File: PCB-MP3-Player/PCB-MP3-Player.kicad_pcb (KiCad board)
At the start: 2 copper layers, 72.6 x 80.8 mm, 26 parts, among them J1 Conn_01x02_Pin, J2 PCM5102A, J3 Oled, J4 Conn_01x06_Pin, J5 Conn_01x02_Pin, J6 Conn_01x03_Pin, J7 Conn_01x03_Pin, SW1 SW_Push, SW2 SW_Push, SW3 SW_Push, SW4 SW_Push, SW5 SW_Push

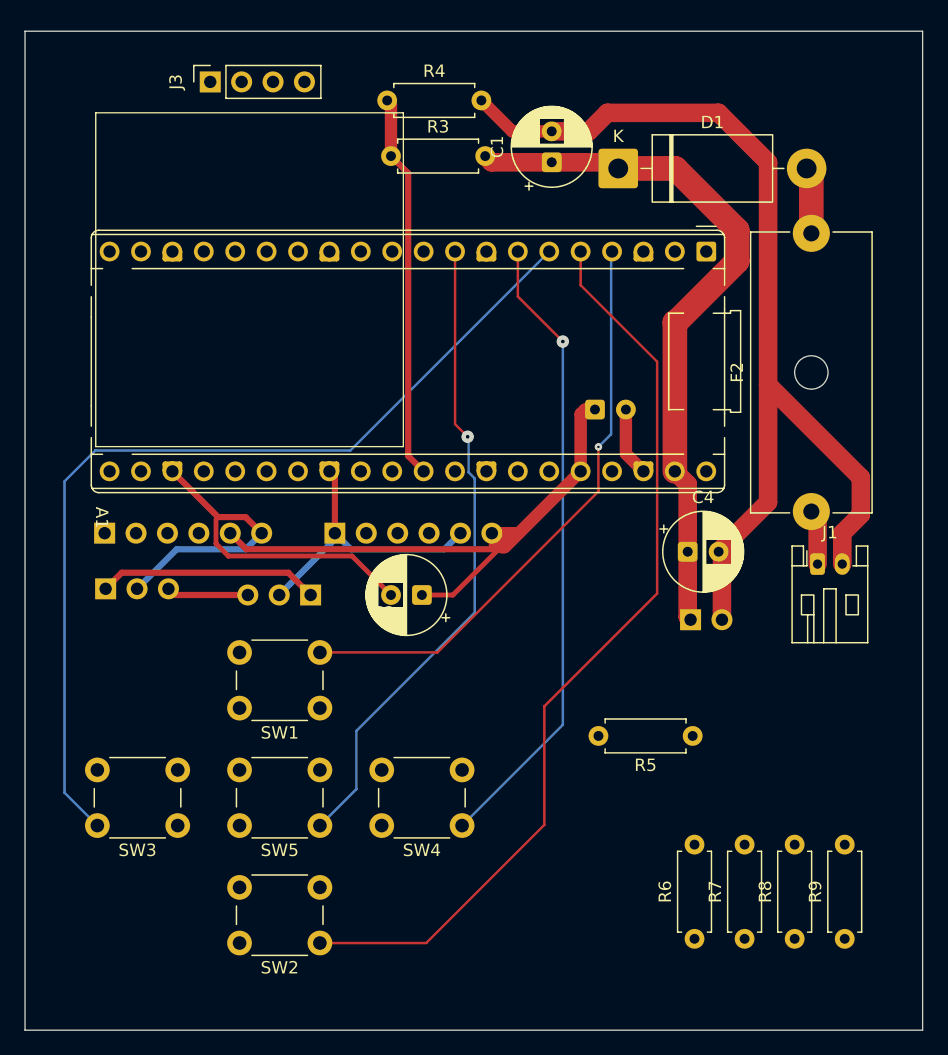
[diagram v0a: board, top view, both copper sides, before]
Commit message: connected oled
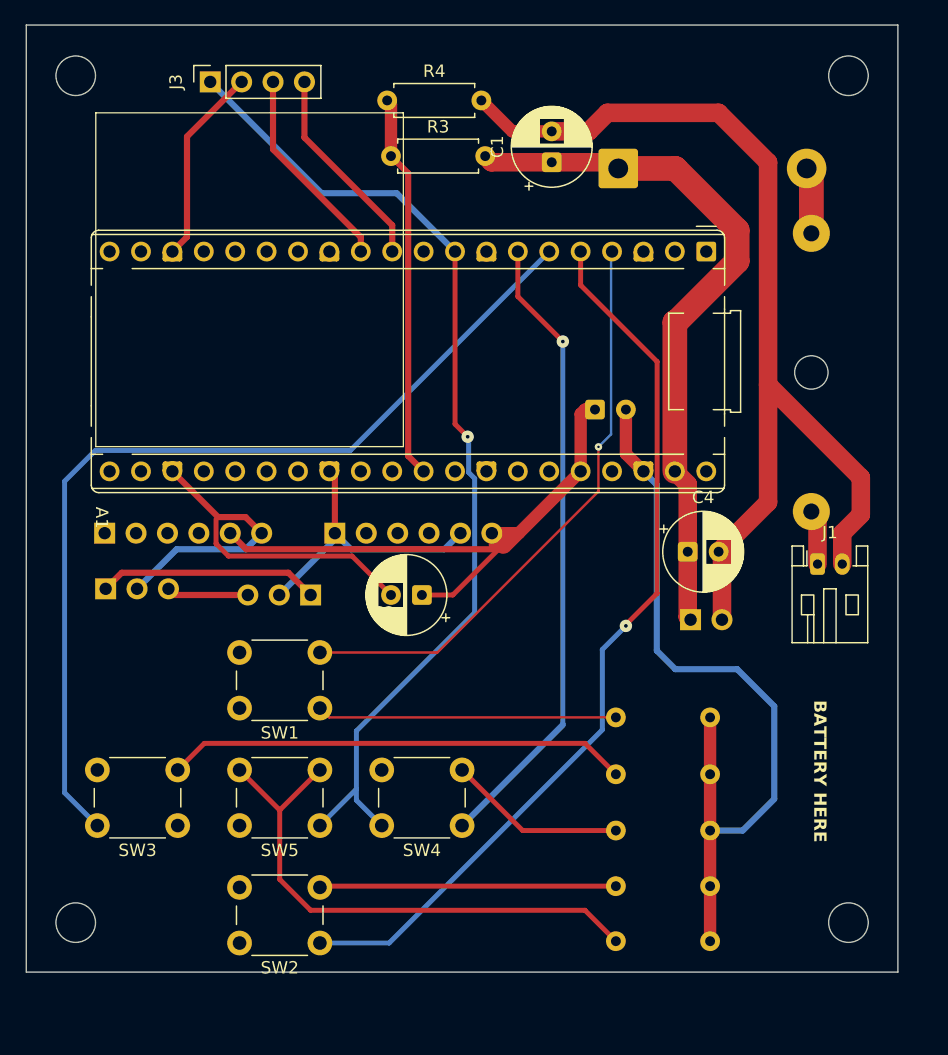
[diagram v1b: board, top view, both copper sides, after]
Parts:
- added REF**: MountingHole_3.2mm_M3_DIN965, MountingHole:MountingHole_3.2mm_M3_DIN965, F.Cu at (132.5, 157.5)
- added REF**: MountingHole_3.2mm_M3_DIN965, MountingHole:MountingHole_3.2mm_M3_DIN965, F.Cu at (195.0, 89.0)
- added REF**: MountingHole_3.2mm_M3_DIN965, MountingHole:MountingHole_3.2mm_M3_DIN965, F.Cu at (195.0, 157.5)
- added REF**: MountingHole_3.2mm_M3_DIN965, MountingHole:MountingHole_3.2mm_M3_DIN965, F.Cu at (132.5, 89.0)
- D1, F2, R5, R6, R7, R8, R9: moved to B.Cu
- moved R9 21.0 mm to (183.8, 140.9), turned to 180 degrees
- moved R5 16.7 mm to (183.8, 159.0)
- moved R8 15.0 mm to (183.8, 145.5), turned to 180 degrees
- moved R7 9.19 mm to (183.8, 150.1), turned to 180 degrees
- moved R6 4.44 mm to (183.8, 154.6), turned to 180 degrees
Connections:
- SW1 pad 1: Net-(R5-Pad2) -> Net-(R9-Pad2)
- SW3 pad 2: Net-(R7-Pad2) -> Net-(R8-Pad2)
- SW4 pad 2: Net-(R8-Pad2) -> Net-(R7-Pad2)
- SW5 pad 2: Net-(R9-Pad2) -> Net-(R5-Pad2)
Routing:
- net GND: track 68.2 -> 142.4 mm
- net Net-(R5-Pad2): track 0.00 -> 44.1 mm
- net Net-(R8-Pad2): track 0.00 -> 37.4 mm
- net +3.3V: track 360.2 -> 387.7 mm, vias 3 -> 4
- net Net-(R9-Pad2): track 0.00 -> 24.3 mm
- net Net-(R6-Pad2): track 0.00 -> 24.0 mm
- net /SDA: track 0.00 -> 16.7 mm
- net /SCL: track 0.00 -> 16.7 mm
- net Net-(R7-Pad2): track 0.00 -> 14.5 mm
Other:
- board size 72.6 x 80.8 mm -> 70.5 x 76.6 mm
- board text added: "BATTERY HERE"

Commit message: pcb changes
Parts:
- removed C4: 100microFarad, Capacitor_THT:CP_Radial_D6.3mm_P2.50mm
- removed J5: Conn_01x02_Pin, Connector_PinSocket_2.54mm:PinSocket_1x02_P2.54mm_Vertical
- removed J6, J7: Conn_01x03_Pin, Connector_PinSocket_2.54mm:PinSocket_1x03_P2.54mm_Vertical
- C1, C2, J1, R3, R4: moved to B.Cu
- C3: moved to F.Cu
- moved R4 7.62 mm to (165.3, 91.0), turned to 180 degrees
- moved C2 2.68 mm to (157.8, 131.0), turned to 0 degrees
- moved J1 2.06 mm to (194.5, 128.0), turned to 180 degrees
- moved R3 0.59 mm to (157.7, 95.0)
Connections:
- C1 pad 2: -BATT -> GND
- C2 pad 1: +3.3V -> GND
- C2 pad 2: GND -> +3.3V
- J1 pad 2: -BATT -> GND
- R4 pad 1: /ADC_BAT -> GND
- R4 pad 2: -BATT -> /ADC_BAT
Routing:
- net -BATT: track 83.5 -> 0.00 mm
- net GND: track 142.4 -> 218.1 mm
- net /L_AUDIO: track 17.9 -> 0.00 mm
- net /LRCK: track 0.00 -> 12.7 mm
- net +BATT: track 57.0 -> 45.0 mm
- net /BCK: track 0.00 -> 10.1 mm
- net /MISO: track 0.00 -> 9.29 mm
- net /SCK: track 0.00 -> 7.55 mm
- net /MOSI: track 0.00 -> 7.55 mm
- net /R_AUDIO: track 6.63 -> 0.00 mm
- net /DIN1: track 0.00 -> 6.23 mm
- net /CS: track 0.00 -> 6.22 mm

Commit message: Devlog #6
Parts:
- A1: moved to B.Cu
- moved A1 50.5 mm to (133.0, 104.0)
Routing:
- net /CS: track 6.22 -> 59.6 mm
- net /SCK: track 7.55 -> 54.6 mm
- net /MISO: track 9.29 -> 46.8 mm
- net /MOSI: track 7.55 -> 38.2 mm
- net +3.3V: track 387.7 -> 415.3 mm, vias 4 -> 5
- net GND: track 218.1 -> 191.2 mm
- net +BATT: track 45.0 -> 63.9 mm
- net /BCK: track 10.1 -> 18.3 mm
- net Net-(R9-Pad2): track 24.3 -> 30.8 mm
- net Net-(R8-Pad2): track 37.4 -> 43.9 mm
- net Net-(R7-Pad2): track 14.5 -> 21.0 mm
- net Net-(R6-Pad2): track 24.0 -> 30.5 mm
- net /LRCK: track 12.7 -> 6.71 mm
- net /SCL: track 16.7 -> 19.7 mm
- net /ADC_BAT: track 31.7 -> 33.7 mm
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
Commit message: Devlog 7
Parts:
- C2: moved to F.Cu
- J4: footprint Connector_PinSocket_2.54mm:PinSocket_1x06_P2.54mm_Vertical -> Connector_JST:JST_SHL_SM06B-SHLS-TF_1x06-1MP_P1.00mm_Horizontal
- moved C2 15.3 mm to (172.0, 125.3), turned to -90 degrees
- moved J4 3.62 mm to (135.6, 129.6)
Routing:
- net +3.3V: track 415.3 -> 441.2 mm
- net GND: track 191.2 -> 211.1 mm
- net /MISO: track 46.8 -> 56.7 mm, vias 0 -> 1
- net /MOSI: track 38.2 -> 45.8 mm, vias 0 -> 1
- net /SCK: track 54.6 -> 57.2 mm, vias 0 -> 1
- net /CS: track 59.6 -> 61.0 mm, vias 0 -> 1

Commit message: Adding renders, readme, etc.
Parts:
- F2: value Littelfuse 02301002H -> 520.620
- J4: footprint Connector_JST:JST_SHL_SM06B-SHLS-TF_1x06-1MP_P1.00mm_Horizontal -> Connector_JST:JST_SH_SM06B-SRSS-TB_1x06-1MP_P1.00mm_Horizontal
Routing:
- net +3.3V: track 441.2 -> 442.1 mm
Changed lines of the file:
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@@
 		)
 	)
-	(footprint "Connector_JST:JST_SHL_SM06B-SHLS-TF_1x06-1MP_P1.00mm_Horizontal"
+	(footprint "Connector_JST:JST_SH_SM06B-SRSS-TB_1x06-1MP_P1.00mm_Horizontal"
 		(layer "B.Cu")
 		(at 135.55 129.55 -90)
-		(descr "JST SHL series connector, SM06B-SHLS-TF (http://www.jst-mfg.com/product/pdf/eng/eSHL.pdf)")
-		(tags "connector JST SHL horizontal")
+		(descr "JST SH series connector, SM06B-SRSS-TB (http://www.jst-mfg.com/product/pdf/eng/eSH.pdf)")
+		(tags "connector JST SH horizontal")
 		(property "Reference" "J4"
-			(at 0 3.5 90)
+			(at 0 3.98 90)
 			(layer "B.SilkS")
 			(effects
@@
 		)
 		(property "Value" "Conn_01x06_Pin"
-			(at 0 -4.2 90)
+			(at 0 -3.98 90)
 			(layer "B.Fab")
 			(effects
@@
 		(duplicate_pad_numbers_are_jumpers no)
 		(fp_line
-			(start -4.51 1.41)
-			(end -3.06 1.41)
+			(start -4.11 1.785)
+			(end -3.06 1.785)
 			(stroke
 				(width 0.12)
@@
 		)
 		(fp_line
-			(start -3.06 1.41)
-			(end -3.06 2.3)
+			(start -3.06 1.785)
+			(end -3.06 2.775)
 			(stroke
 				(width 0.12)
@@
 		)
 		(fp_line
-			(start 4.51 1.41)
-			(end 3.06 1.41)
+			(start 4.11 1.785)
+			(end 3.06 1.785)
 			(stroke
 				(width 0.12)
@@
 		)
 		(fp_line
-			(start -4.51 -0.34)
-			(end -4.51 1.41)
+			(start -4.11 -0.715)
+			(end -4.11 1.785)
 			(stroke
 				(width 0.12)
@@
 		)
 		(fp_line
-			(start 4.51 -0.34)
-			(end 4.51 1.41)
+			(start 4.11 -0.715)
+			(end 4.11 1.785)
 			(stroke
 				(width 0.12)
@@
 		)
 		(fp_line
-			(start -4.51 -2.56)
-			(end -4.51 -3.11)
+			(start -2.94 -2.685)
+			(end 2.94 -2.685)
 			(stroke
 				(width 0.12)
@@
 		)
 		(fp_line
-			(start -4.51 -3.11)
-			(end 4.51 -3.11)
+			(start -3.3 3.28)
+			(end 3.3 3.28)
 			(stroke
-				(width 0.12)
+				(width 0.05)
 				(type solid)
 			)
-			(layer "B.SilkS")
+			(layer "B.CrtYd")
 		)
 		(fp_line
-			(start 4.51 -3.11)
-			(end 4.51 -2.56)
+			(start 3.3 3.28)
+			(end 3.3 2.18)
 			(stroke
-				(width 0.12)
+				(width 0.05)
 				(type solid)
 			)
-			(layer "B.SilkS")
+			(layer "B.CrtYd")
+		)
+		(fp_line
+			(start -4.5 2.18)
+			(end -3.3 2.18)
+			(stroke
+				(width 0.05)
+				(type solid)
+			)
+			(layer "B.CrtYd")
+		)
+		(fp_line
+			(start -3.3 2.18)
+			(end -3.3 3.28)
+			(stroke
+				(width 0.05)
+				(type solid)
+			)
+			(layer "B.CrtYd")
+		)
+		(fp_line
+			(start 3.3 2.18)
+			(end 4.5 2.18)
+			(stroke
+				(width 0.05)
+				(type solid)
+			)
+			(layer "B.CrtYd")
+		)
+		(fp_line
+			(start 4.5 2.18)
+			(end 4.5 -0.47)
+			(stroke
+				(width 0.05)
+				(type solid)
+			)
+			(layer "B.CrtYd")
+		)
+		(fp_line
+			(start -4.9 -0.47)
+			(end -4.5 -0.47)
+			(stroke
+				(width 0.05)
+				(type solid)
+			)
+			(layer "B.CrtYd")
 		)
 		(fp_line
-			(start -3.3 2.8)
-			(end 3.3 2.8)
+			(start -4.5 -0.47)
+			(end -4.5 2.18)
 			(stroke
 				(width 0.05)
@@
 		)
 		(fp_line
-			(start 3.3 2.8)
-			(end 3.3 1.8)
+			(start 4.5 -0.47)
+			(end 4.9 -0.47)
 			(stroke
 				(width 0.05)
@@
 		)
 		(fp_line
-			(start -4.9 1.8)
-			(end -3.3 1.8)
+			(start 4.9 -0.47)
+			(end 4.9 -3.28)
 			(stroke
 				(width 0.05)
@@
 		)
 		(fp_line
-			(start -3.3 1.8)
-			(end -3.3 2.8)
+			(start -2.69 -3.08)
+			(end -2.69 -3.28)
 			(stroke
 				(width 0.05)
@@
 		)
 		(fp_line
-			(start 3.3 1.8)
-			(end 4.9 1.8)
+			(start 2.69 -3.08)
+			(end -2.69 -3.08)
 			(stroke
 				(width 0.05)
@@
 		)
 		(fp_line
-			(start 4.9 1.8)
-			(end 4.9 -3.5)
+			(start -4.9 -3.28)
+			(end -4.9 -0.47)
 			(stroke
 				(width 0.05)
@@
 		)
 		(fp_line
-			(start -4.9 -3.5)
-			(end -4.9 1.8)
+			(start -2.69 -3.28)
+			(end -4.9 -3.28)
 			(stroke
 				(width 0.05)
@@
 		)
 		(fp_line
-			(start 4.9 -3.5)
-			(end -4.9 -3.5)
+			(start 2.69 -3.28)
+			(end 2.69 -3.08)
 			(stroke
 				(width 0.05)
@@
 		)
 		(fp_line
-			(start -4.4 1.3)
-			(end 4.4 1.3)
+			(start 4.9 -3.28)
+			(end 2.69 -3.28)
+			(stroke
+				(width 0.05)
+				(type solid)
+			)
+			(layer "B.CrtYd")
+		)
+		(fp_line
+			(start -4 1.675)
+			(end 4 1.675)
 			(stroke
 				(width 0.1)
@@
 		)
 		(fp_line
-			(start -4.4 1.3)
-			(end -4.4 -3)
+			(start -4 1.675)
+			(end -4 -2.575)
 			(stroke
 				(width 0.1)
@@
 		)
 		(fp_line
-			(start -3 1.3)
-			(end -2.5 0.592893)
+			(start -3 1.675)
+			(end -2.5 0.967893)
 			(stroke
 				(width 0.1)
@@
 		)
 		(fp_line
-			(start 4.4 1.3)
-			(end 4.4 -3)
+			(start 4 1.675)
+			(end 4 -2.575)
 			(stroke
 				(width 0.1)
@@
 		)
 		(fp_line
-			(start -2.5 0.592893)
-			(end -2 1.3)
+			(start -2.5 0.967893)
+			(end -2 1.675)
 			(stroke
 				(width 0.1)
@@
 		)
 		(fp_line
-			(start -4.4 -3)
-			(end 4.4 -3)
+			(start -4 -2.575)
+			(end 4 -2.575)
 			(stroke
 				(width 0.1)
@@
 		)
 		(fp_text user "${REFERENCE}"
-			(at 0 -0.5 90)
+			(at 0 0 90)
 			(layer "B.Fab")
 			(effects
@@
 		)
 		(pad "1" smd roundrect
-			(at -2.5 1.675 270)
-			(size 0.6 1.25)
+			(at -2.5 2 270)
+			(size 0.6 1.55)
 			(layers "B.Cu" "B.Mask" "B.Paste")
 			(roundrect_rratio 0.25)
@@
 		)
 		(pad "2" smd roundrect
-			(at -1.5 1.675 270)
-			(size 0.6 1.25)
+			(at -1.5 2 270)
+			(size 0.6 1.55)
 			(layers "B.Cu" "B.Mask" "B.Paste")
 			(roundrect_rratio 0.25)
@@
 		)
 		(pad "3" smd roundrect
-			(at -0.5 1.675 270)
-			(size 0.6 1.25)
+			(at -0.5 2 270)
+			(size 0.6 1.55)
 			(layers "B.Cu" "B.Mask" "B.Paste")
 			(roundrect_rratio 0.25)
@@
 		)
 		(pad "4" smd roundrect
-			(at 0.5 1.675 270)
-			(size 0.6 1.25)
+			(at 0.5 2 270)
+			(size 0.6 1.55)
 			(layers "B.Cu" "B.Mask" "B.Paste")
 			(roundrect_rratio 0.25)
@@
 		)
 		(pad "5" smd roundrect
-			(at 1.5 1.675 270)
-			(size 0.6 1.25)
+			(at 1.5 2 270)
+			(size 0.6 1.55)
 			(layers "B.Cu" "B.Mask" "B.Paste")
 			(roundrect_rratio 0.25)
@@
 		)
 		(pad "6" smd roundrect
-			(at 2.5 1.675 270)
-			(size 0.6 1.25)
+			(at 2.5 2 270)
+			(size 0.6 1.55)
 			(layers "B.Cu" "B.Mask" "B.Paste")
 			(roundrect_rratio 0.25)
@@
 		)
 		(pad "MP" smd roundrect
-			(at -3.95 -1.45 270)
-			(size 0.9 1.7)
+			(at -3.8 -1.875 270)
+			(size 1.2 1.8)
 			(layers "B.Cu" "B.Mask" "B.Paste")
-			(roundrect_rratio 0.25)
+			(roundrect_rratio 0.208333)
 		)
 		(pad "MP" smd roundrect
-			(at 3.95 -1.45 270)
-			(size 0.9 1.7)
+			(at 3.8 -1.875 270)
+			(size 1.2 1.8)
 			(layers "B.Cu" "B.Mask" "B.Paste")
-			(roundrect_rratio 0.25)
+			(roundrect_rratio 0.208333)
 		)
 		(embedded_fonts no)
-		(model "${KICAD10_3DMODEL_DIR}/Connector_JST.3dshapes/JST_SHL_SM06B-SHLS-TF_1x06-1MP_P1.00mm_Horizontal.step"
+		(model "${KICAD10_3DMODEL_DIR}/Connector_JST.3dshapes/JST_SH_SM06B-SRSS-TB_1x06-1MP_P1.00mm_Horizontal.step"
 			(offset
 				(xyz 0 0 0)
@@
 			)
 		)
-		(property "Value" "Littelfuse 02301002H"
+		(property "Value" "520.620"
 			(at 11.25 -6 90)
 			(layer "B.Fab")
@@
 	)
 	(segment
-		(start 132.5 130.299999)
-		(end 132.5 126.5)
-		(width 0.5)
-		(layer "B.Cu")
-		(net "+3.3V")
-	)
-	(segment
 		(start 155 134.5)
 		(end 155 135.5)
@@
 	)
 	(segment
+		(start 132.7 131.05)
+		(end 133.55 131.05)
+		(width 0.4)
+		(layer "B.Cu")
+		(net "+3.3V")
+	)
+	(segment
 		(start 132.5 126.5)
 		(end 135.1 123.9)
@@
 	)
 	(segment
-		(start 133.250001 131.05)
-		(end 132.5 130.299999)
-		(width 0.5)
-		(layer "B.Cu")
-		(net "+3.3V")
-	)
-	(segment
 		(start 155 135.5)
 		(end 154 136.5)
@@
 	)
 	(segment
+		(start 132.15 126.85)
+		(end 132.15 130.5)
+		(width 0.5)
+		(layer "B.Cu")
+		(net "+3.3V")
+	)
+	(segment
 		(start 166.16 127.34)
 		(end 166.16 126)
@@
 	)
 	(segment
+		(start 132.15 130.5)
+		(end 132.7 131.05)
+		(width 0.5)
+		(layer "B.Cu")
+		(net "+3.3V")
+	)
+	(segment
 		(start 142.5 89.5)
 		(end 143.38 89.5)
@@
 		(layer "B.Cu")
 		(net "+3.3V")
+	)
+	(segment
+		(start 132.5 126.5)
+		(end 132.15 126.85)
+		(width 0.4)
+		(layer "B.Cu")
+		(net "+3.3V")
